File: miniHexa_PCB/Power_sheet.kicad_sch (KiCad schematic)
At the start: 34 parts, among them J2 12v DC, U2 HT7333, U3 RT8289GSP, U4 BQ25886RGE

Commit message: update
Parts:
- removed U2: HT7333, Package_TO_SOT_SMD:SOT-89-3, symbol Regulator_Linear:HT75xx-1-SOT89
- added U6: AMS1117-3.3, Package_TO_SOT_SMD:SOT-223-3_TabPin2, symbol Regulator_Linear:AMS1117-3.3
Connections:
- net +3.3V: now also U6.2 (VO)
- net +5V: now also U6.3 (VI)
- net GND: now also U6.1 (GND)

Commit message: simple update
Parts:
- C11, C12, C14, C15, C16, C17, C18, C19, C20, C21, C22, C23, C24: footprint Capacitor_SMD:C_0805_2012Metric -> Capacitor_SMD:C_0402_1005Metric
- C25: value C -> 4.7uF; footprint Capacitor_SMD:C_0805_2012Metric -> Capacitor_SMD:C_0402_1005Metric
- L1, L2: footprint Inductor_SMD:L_APV_APH0850 -> Inductor_SMD:L_Panasonic_PCC-M0850M
- R27, R28: value R -> 2.2k
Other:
- moved on the sheet: C25
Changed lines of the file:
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@@
 	)
 	(junction
+		(at 257.81 45.72)
+		(diameter 0)
+		(color 0 0 0 0)
+	)
+	(junction
 		(at 52.07 173.99)
 		(diameter 0)
@@
 	)
 	(junction
-		(at 257.81 45.72)
-		(diameter 0)
-		(color 0 0 0 0)
-	)
-	(junction
 		(at 269.24 45.72)
 		(diameter 0)
@@
 	(wire
 		(pts
-			(xy 186.69 55.88) (xy 203.2 55.88)
+			(xy 195.58 55.88) (xy 203.2 55.88)
 		)
 		(stroke
@@
 			)
 		)
-		(property "Footprint" "Capacitor_SMD:C_0805_2012Metric"
+		(property "Footprint" "Capacitor_SMD:C_0402_1005Metric"
 			(at 54.3052 41.91 0)
 			(hide yes)
@@
 			)
 		)
-		(property "Footprint" "Capacitor_SMD:C_0805_2012Metric"
+		(property "Footprint" "Capacitor_SMD:C_0402_1005Metric"
 			(at 73.9648 111.76 0)
 			(hide yes)
@@
 			)
 		)
-		(property "Footprint" "Inductor_SMD:L_APV_APH0850"
+		(property "Footprint" "Inductor_SMD:L_Panasonic_PCC-M0850M"
 			(at 87.63 137.16 0)
 			(hide yes)
@@
 			)
 		)
-		(property "Value" "R"
+		(property "Value" "2.2k"
 			(at 246.38 36.83 90)
 			(show_name no)
@@
 			)
 		)
-		(property "Footprint" "Inductor_SMD:L_APV_APH0850"
+		(property "Footprint" "Inductor_SMD:L_Panasonic_PCC-M0850M"
 			(at 170.18 46.99 0)
 			(hide yes)
@@
 			)
 		)
-		(property "Footprint" "Capacitor_SMD:C_0805_2012Metric"
+		(property "Footprint" "Capacitor_SMD:C_0402_1005Metric"
 			(at 129.54 148.8948 0)
 			(hide yes)
@@
 			)
 		)
-		(property "Footprint" "Capacitor_SMD:C_0805_2012Metric"
+		(property "Footprint" "Capacitor_SMD:C_0402_1005Metric"
 			(at 51.1048 151.13 0)
 			(hide yes)
@@
 			)
 		)
-		(property "Footprint" "Capacitor_SMD:C_0805_2012Metric"
+		(property "Footprint" "Capacitor_SMD:C_0402_1005Metric"
 			(at 62.5348 151.13 0)
 			(hide yes)
@@
 			)
 		)
-		(property "Footprint" "Capacitor_SMD:C_0805_2012Metric"
+		(property "Footprint" "Capacitor_SMD:C_0402_1005Metric"
 			(at 268.2748 45.72 0)
 			(hide yes)
@@
 		(dnp no)
 		(property "Reference" "C20"
-			(at 250.952 48.514 0)
-			(hide yes)
+			(at 252.476 47.752 0)
 			(show_name no)
 			(do_not_autoplace no)
@@
 		)
 		(property "Value" "22uF"
-			(at 251.206 50.8 0)
-			(hide yes)
+			(at 252.73 50.038 0)
 			(show_name no)
 			(do_not_autoplace no)
@@
 			)
 		)
-		(property "Footprint" "Capacitor_SMD:C_0805_2012Metric"
+		(property "Footprint" "Capacitor_SMD:C_0402_1005Metric"
 			(at 256.8448 45.72 0)
 			(hide yes)
@@
 			)
 		)
-		(property "Footprint" "Capacitor_SMD:C_0805_2012Metric"
+		(property "Footprint" "Capacitor_SMD:C_0402_1005Metric"
 			(at 33.9852 41.91 0)
 			(hide yes)
@@
 			)
 		)
-		(property "Footprint" "Capacitor_SMD:C_0805_2012Metric"
+		(property "Footprint" "Capacitor_SMD:C_0402_1005Metric"
 			(at 239.7252 58.42 0)
 			(hide yes)
@@
 	(symbol
 		(lib_id "Device:C")
-		(at 186.69 59.69 0)
+		(at 195.58 59.69 0)
 		(unit 1)
 		(body_style 1)
@@
 		(fields_autoplaced yes)
 		(property "Reference" "C25"
-			(at 190.5 58.4199 0)
+			(at 199.39 58.4199 0)
 			(show_name no)
 			(do_not_autoplace no)
@@
 			)
 		)
-		(property "Value" "C"
-			(at 190.5 60.9599 0)
+		(property "Value" "4.7uF"
+			(at 199.39 60.9599 0)
 			(show_name no)
 			(do_not_autoplace no)
@@
 			)
 		)
-		(property "Footprint" "Capacitor_SMD:C_0805_2012Metric"
-			(at 187.6552 63.5 0)
+		(property "Footprint" "Capacitor_SMD:C_0402_1005Metric"
+			(at 196.5452 63.5 0)
 			(hide yes)
 			(show_name no)
@@
 		)
 		(property "Datasheet" ""
-			(at 186.69 59.69 0)
+			(at 195.58 59.69 0)
 			(hide yes)
 			(show_name no)
@@
 		)
 		(property "Description" "Unpolarized capacitor"
-			(at 186.69 59.69 0)
+			(at 195.58 59.69 0)
 			(hide yes)
 			(show_name no)
@@
 			)
 		)
-		(property "Value" "R"
+		(property "Value" "2.2k"
 			(at 246.38 40.64 90)
 			(show_name no)
@@
 	(symbol
 		(lib_id "power:GND")
-		(at 186.69 63.5 0)
+		(at 195.58 63.5 0)
 		(unit 1)
 		(body_style 1)
@@
 		(fields_autoplaced yes)
 		(property "Reference" "#PWR031"
-			(at 186.69 69.85 0)
+			(at 195.58 69.85 0)
 			(hide yes)
 			(show_name no)
@@
 		)
 		(property "Value" "GND"
-			(at 186.69 68.58 0)
+			(at 195.58 68.58 0)
 			(show_name no)
 			(do_not_autoplace no)
@@
 		)
 		(property "Footprint" ""
-			(at 186.69 63.5 0)
+			(at 195.58 63.5 0)
 			(hide yes)
 			(show_name no)
@@
 		)
 		(property "Datasheet" ""
-			(at 186.69 63.5 0)
+			(at 195.58 63.5 0)
 			(hide yes)
 			(show_name no)
@@
 		)
 		(property "Description" "Power symbol creates a global label with name \"GND\" , ground"
-			(at 186.69 63.5 0)
+			(at 195.58 63.5 0)
 			(hide yes)
 			(show_name no)
@@
 			)
 		)
-		(property "Footprint" "Capacitor_SMD:C_0805_2012Metric"
+		(property "Footprint" "Capacitor_SMD:C_0402_1005Metric"
 			(at 170.18 42.2148 0)
 			(hide yes)
@@
 			)
 		)
-		(property "Footprint" "Capacitor_SMD:C_0805_2012Metric"
+		(property "Footprint" "Capacitor_SMD:C_0402_1005Metric"
 			(at 39.0652 158.75 0)
 			(hide yes)
@@
 			)
 		)
-		(property "Footprint" "Capacitor_SMD:C_0805_2012Metric"
+		(property "Footprint" "Capacitor_SMD:C_0402_1005Metric"
 			(at 85.3948 111.76 0)
 			(hide yes)
@@
 			)
 		)
-		(property "Footprint" "Capacitor_SMD:C_0805_2012Metric"
+		(property "Footprint" "Capacitor_SMD:C_0402_1005Metric"
 			(at 171.1452 58.42 0)
 			(hide yes)

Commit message: layout phase pcb
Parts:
- C19: footprint Capacitor_SMD:C_0402_1005Metric -> Capacitor_SMD:CP_Elec_6.3x7.7
- C22: value C -> 10uF
- C24: value C -> 47nF
- R22, R23, R24, R25, R26, R27, R28, R30, R31: footprint Resistor_SMD:R_0805_2012Metric -> Resistor_SMD:R_0402_1005Metric
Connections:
- net GND: now also C25.1, U4.5 (OTG); no longer C25.2
- net at U4.11 (REGN): now also C25.2; no longer C25.1
- no-connect marks 7 -> 6
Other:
- moved on the sheet: C25
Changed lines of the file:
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@@
 		(at 203.2 59.69)
 	)
-	(no_connect
-		(at 203.2 64.77)
-	)
 	(wire
 		(pts
@@
 			)
 		)
-		(property "Footprint" "Resistor_SMD:R_0805_2012Metric"
+		(property "Footprint" "Resistor_SMD:R_0402_1005Metric"
 			(at 65.532 38.1 90)
 			(hide yes)
@@
 			)
 		)
-		(property "Footprint" "Resistor_SMD:R_0805_2012Metric"
+		(property "Footprint" "Resistor_SMD:R_0402_1005Metric"
 			(at 246.38 38.608 90)
 			(hide yes)
@@
 			)
 		)
-		(property "Footprint" "Resistor_SMD:R_0805_2012Metric"
+		(property "Footprint" "Resistor_SMD:R_0402_1005Metric"
 			(at 196.85 84.328 90)
 			(hide yes)
@@
 	(symbol
 		(lib_id "power:GND")
+		(at 203.2 64.77 270)
+		(unit 1)
+		(body_style 1)
+		(exclude_from_sim no)
+		(in_bom yes)
+		(on_board yes)
+		(in_pos_files yes)
+		(dnp no)
+		(fields_autoplaced yes)
+		(property "Reference" "#PWR032"
+			(at 196.85 64.77 0)
+			(hide yes)
+			(show_name no)
+			(do_not_autoplace no)
+			(effects
+				(font
+					(size 1.27 1.27)
+				)
+			)
+		)
+		(property "Value" "GND"
+			(at 199.39 64.7699 90)
+			(show_name no)
+			(do_not_autoplace no)
+			(effects
+				(font
+					(size 1.27 1.27)
+				)
+				(justify right)
+			)
+		)
+		(property "Footprint" ""
+			(at 203.2 64.77 0)
+			(hide yes)
+			(show_name no)
+			(do_not_autoplace no)
+			(effects
+				(font
+					(size 1.27 1.27)
+				)
+			)
+		)
+		(property "Datasheet" ""
+			(at 203.2 64.77 0)
+			(hide yes)
+			(show_name no)
+			(do_not_autoplace no)
+			(effects
+				(font
+					(size 1.27 1.27)
+				)
+			)
+		)
+		(property "Description" "Power symbol creates a global label with name \"GND\" , ground"
+			(at 203.2 64.77 0)
+			(hide yes)
+			(show_name no)
+			(do_not_autoplace no)
+			(effects
+				(font
+					(size 1.27 1.27)
+				)
+			)
+		)
+		(pin "1"
+		)
+		(instances
+			(project "miniHexa"
+				(path "/3449ee66-2977-4802-a474-0821cdf4e79b/33698118-31e2-44d0-a5be-b46ca646d44a"
+					(reference "#PWR032")
+					(unit 1)
+				)
+			)
+		)
+	)
+	(symbol
+		(lib_id "power:GND")
 		(at 238.76 58.42 0)
 		(unit 1)
@@
 			)
 		)
-		(property "Value" "C"
+		(property "Value" "10uF"
 			(at 233.426 55.372 0)
 			(show_name no)
@@
 	(symbol
 		(lib_id "Device:C")
-		(at 195.58 59.69 0)
+		(at 191.77 55.88 90)
 		(unit 1)
 		(body_style 1)
@@
 		(fields_autoplaced yes)
 		(property "Reference" "C25"
-			(at 199.39 58.4199 0)
+			(at 191.77 48.26 90)
 			(show_name no)
 			(do_not_autoplace no)
@@
 					(size 1.27 1.27)
 				)
-				(justify left)
 			)
 		)
 		(property "Value" "4.7uF"
-			(at 199.39 60.9599 0)
+			(at 191.77 50.8 90)
 			(show_name no)
 			(do_not_autoplace no)
@@
 					(size 1.27 1.27)
 				)
-				(justify left)
 			)
 		)
 		(property "Footprint" "Capacitor_SMD:C_0402_1005Metric"
-			(at 196.5452 63.5 0)
+			(at 195.58 54.9148 0)
 			(hide yes)
 			(show_name no)
@@
 		)
 		(property "Datasheet" ""
-			(at 195.58 59.69 0)
+			(at 191.77 55.88 0)
 			(hide yes)
 			(show_name no)
@@
 		)
 		(property "Description" "Unpolarized capacitor"
-			(at 195.58 59.69 0)
+			(at 191.77 55.88 0)
 			(hide yes)
 			(show_name no)
@@
 			)
 		)
-		(property "Footprint" "Resistor_SMD:R_0805_2012Metric"
+		(property "Footprint" "Resistor_SMD:R_0402_1005Metric"
 			(at 246.38 42.418 90)
 			(hide yes)
@@
 			)
 		)
-		(property "Footprint" "Resistor_SMD:R_0805_2012Metric"
+		(property "Footprint" "Resistor_SMD:R_0402_1005Metric"
 			(at 71.882 162.56 90)
 			(hide yes)
@@
 	(symbol
 		(lib_id "power:GND")
-		(at 195.58 63.5 0)
+		(at 187.96 55.88 0)
 		(unit 1)
 		(body_style 1)
@@
 		(fields_autoplaced yes)
 		(property "Reference" "#PWR031"
-			(at 195.58 69.85 0)
+			(at 187.96 62.23 0)
 			(hide yes)
 			(show_name no)
@@
 		)
 		(property "Value" "GND"
-			(at 195.58 68.58 0)
+			(at 187.96 60.96 0)
 			(show_name no)
 			(do_not_autoplace no)
@@
 		)
 		(property "Footprint" ""
-			(at 195.58 63.5 0)
+			(at 187.96 55.88 0)
 			(hide yes)
 			(show_name no)
@@
 		)
 		(property "Datasheet" ""
-			(at 195.58 63.5 0)
+			(at 187.96 55.88 0)
 			(hide yes)
 			(show_name no)
@@
 		)
 		(property "Description" "Power symbol creates a global label with name \"GND\" , ground"
-			(at 195.58 63.5 0)
+			(at 187.96 55.88 0)
 			(hide yes)
 			(show_name no)
@@
 			)
 		)
-		(property "Footprint" "Resistor_SMD:R_0805_2012Metric"
+		(property "Footprint" "Resistor_SMD:R_0402_1005Metric"
 			(at 71.882 147.32 90)
 			(hide yes)
@@
 			)
 		)
-		(property "Footprint" "Resistor_SMD:R_0805_2012Metric"
+		(property "Footprint" "Resistor_SMD:R_0402_1005Metric"
 			(at 125.73 106.172 90)
 			(hide yes)
@@
 			)
 		)
-		(property "Footprint" "Resistor_SMD:R_0805_2012Metric"
+		(property "Footprint" "Resistor_SMD:R_0402_1005Metric"
 			(at 196.85 79.248 90)
 			(hide yes)
@@
 			)
 		)
-		(property "Footprint" "Capacitor_SMD:C_0402_1005Metric"
+		(property "Footprint" "Capacitor_SMD:CP_Elec_6.3x7.7"
 			(at 39.0652 158.75 0)
 			(hide yes)
@@
 			)
 		)
-		(property "Footprint" "Resistor_SMD:R_0805_2012Metric"
+		(property "Footprint" "Resistor_SMD:R_0402_1005Metric"
 			(at 196.85 74.168 90)
 			(hide yes)
@@
 			)
 		)
-		(property "Value" "C"
+		(property "Value" "47nF"
 			(at 162.814 55.372 0)
 			(show_name no)

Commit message: before auto routing
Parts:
- added C2: 22uF, Capacitor_SMD:C_0402_1005Metric, symbol Device:C
- added C27: 100nF, Capacitor_SMD:C_0402_1005Metric, symbol Device:C
- BT1: footprint Battery:BatteryHolder_Keystone_2468_2xAAA -> Connector_JST:JST_XH_S2B-XH-A-1_1x02_P2.50mm_Horizontal
- C23: value C -> 10uF
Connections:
- net GND: now also C2.1, C27.1
- net at J2.1, U4.23 (VBUS): now also C2.2, C27.2

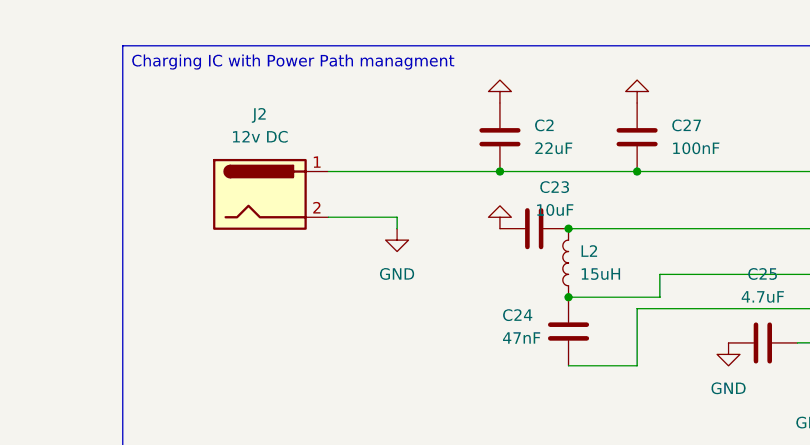
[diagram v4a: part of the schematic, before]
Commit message: added water marks
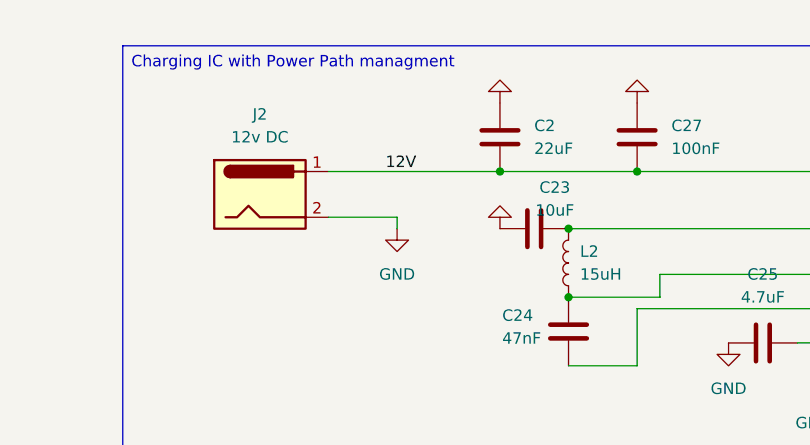
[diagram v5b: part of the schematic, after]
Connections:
- net 12V: now reaches C2.2, C27.2, J2.1, U4.23 (VBUS)
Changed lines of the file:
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@@
+		)
+	)
+	(label "12V"
+		(at 149.8505 36.83 0)
+		(effects
+			(font
+				(size 1.27 1.27)
+			)
+			(justify left bottom)
 		)
 	)

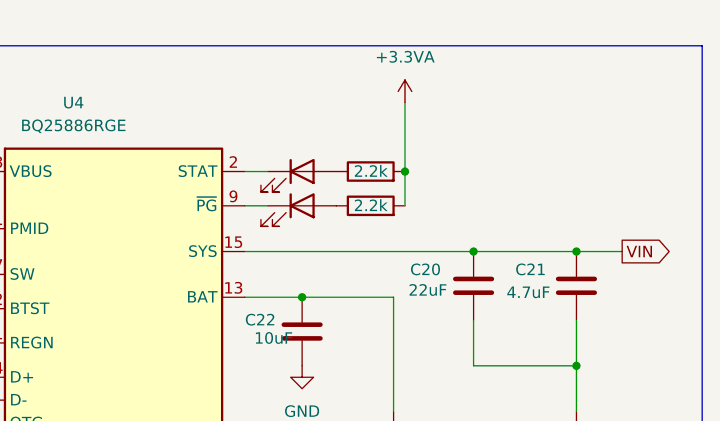
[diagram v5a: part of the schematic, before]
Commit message: updated some power lines
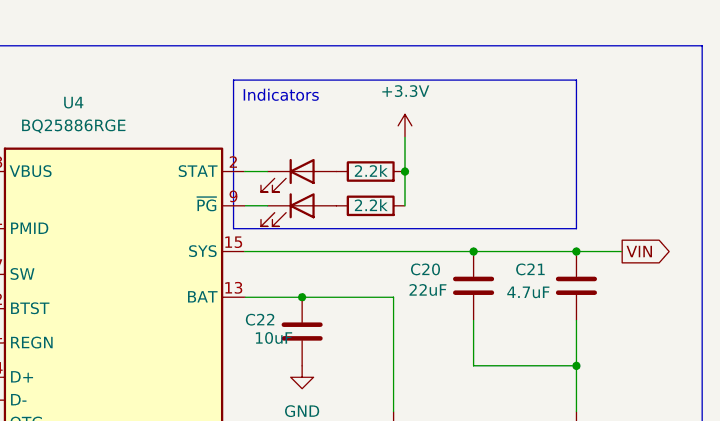
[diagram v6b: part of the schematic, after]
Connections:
- net +3.3VA is gone; now on net +3.3V: R27.2, R28.2
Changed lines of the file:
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@@
 		)
 	)
+	(text_box "Indicators"
+		(exclude_from_sim no)
+		(at 231.14 26.67 0)
+		(size 38.1 16.51)
+		(margins 0.9525 0.9525 0.9525 0.9525)
+		(stroke
+			(width 0)
+			(type solid)
+		)
+		(fill
+			(type none)
+		)
+		(effects
+			(font
+				(size 1.27 1.27)
+			)
+			(justify left top)
+		)
+	)
 	(junction
 		(at 53.34 41.91)
@@
 	)
 	(junction
-		(at 162.56 36.83)
+		(at 250.19 36.83)
 		(diameter 0)
 		(color 0 0 0 0)
 	)
 	(junction
-		(at 170.18 50.8)
+		(at 162.56 36.83)
 		(diameter 0)
 		(color 0 0 0 0)
 	)
 	(junction
-		(at 63.5 173.99)
+		(at 170.18 50.8)
 		(diameter 0)
 		(color 0 0 0 0)
 	)
 	(junction
-		(at 269.24 58.42)
+		(at 63.5 173.99)
 		(diameter 0)
 		(color 0 0 0 0)
 	)
 	(junction
-		(at 250.19 36.83)
+		(at 269.24 58.42)
 		(diameter 0)
 		(color 0 0 0 0)
@@
 	(wire
 		(pts
-			(xy 250.19 29.21) (xy 250.19 36.83)
+			(xy 250.19 33.02) (xy 250.19 36.83)
 		)
 		(stroke
@@
 	)
 	(symbol
+		(lib_id "power:+3.3V")
+		(at 250.19 33.02 0)
+		(unit 1)
+		(body_style 1)
+		(exclude_from_sim no)
+		(in_bom yes)
+		(on_board yes)
+		(in_pos_files yes)
+		(dnp no)
+		(fields_autoplaced yes)
+		(property "Reference" "#PWR022"
+			(at 250.19 36.83 0)
+			(hide yes)
+			(show_name no)
+			(do_not_autoplace no)
+			(effects
+				(font
+					(size 1.27 1.27)
+				)
+			)
+		)
+		(property "Value" "+3.3V"
+			(at 250.19 27.94 0)
+			(show_name no)
+			(do_not_autoplace no)
+			(effects
+				(font
+					(size 1.27 1.27)
+				)
+			)
+		)
+		(property "Footprint" ""
+			(at 250.19 33.02 0)
+			(hide yes)
+			(show_name no)
+			(do_not_autoplace no)
+			(effects
+				(font
+					(size 1.27 1.27)
+				)
+			)
+		)
+		(property "Datasheet" ""
+			(at 250.19 33.02 0)
+			(hide yes)
+			(show_name no)
+			(do_not_autoplace no)
+			(effects
+				(font
+					(size 1.27 1.27)
+				)
+			)
+		)
+		(property "Description" "Power symbol creates a global label with name \"+3.3V\""
+			(at 250.19 33.02 0)
+			(hide yes)
+			(show_name no)
+			(do_not_autoplace no)
+			(effects
+				(font
+					(size 1.27 1.27)
+				)
+			)
+		)
+		(pin "1"
+		)
+		(instances
+			(project "miniHexa"
+				(path "/3449ee66-2977-4802-a474-0821cdf4e79b/33698118-31e2-44d0-a5be-b46ca646d44a"
+					(reference "#PWR022")
+					(unit 1)
+				)
+			)
+		)
+	)
+	(symbol
 		(lib_id "Device:L")
 		(at 87.63 137.16 90)
@@
 					(unit 1)
 				)
-			)
-		)
-	)
-	(symbol
-		(lib_id "power:+3.3VA")
-		(at 250.19 29.21 0)
-		(unit 1)
-		(body_style 1)
-		(exclude_from_sim no)
-		(in_bom yes)
-		(on_board yes)
-		(in_pos_files yes)
-		(dnp no)
-		(fields_autoplaced yes)
-		(property "Reference" "#PWR028"
-			(at 250.19 33.02 0)
-			(hide yes)
-			(show_name no)
-			(do_not_autoplace no)
-			(effects
-				(font
-					(size 1.27 1.27)
-				)
-			)
-		)
-		(property "Value" "+3.3VA"
-			(at 250.19 24.13 0)
-			(show_name no)
-			(do_not_autoplace no)
-			(effects
-				(font
-					(size 1.27 1.27)
-				)
-			)
-		)
-		(property "Footprint" ""
-			(at 250.19 29.21 0)
-			(hide yes)
-			(show_name no)
-			(do_not_autoplace no)
-			(effects
-				(font
-					(size 1.27 1.27)
-				)
-			)
-		)
-		(property "Datasheet" ""
-			(at 250.19 29.21 0)
-			(hide yes)
-			(show_name no)
-			(do_not_autoplace no)
-			(effects
-				(font
-					(size 1.27 1.27)
-				)
-			)
-		)
-		(property "Description" "Power symbol creates a global label with name \"+3.3VA\""
-			(at 250.19 29.21 0)
-			(hide yes)
-			(show_name no)
-			(do_not_autoplace no)
-			(effects
-				(font
-					(size 1.27 1.27)
-				)
-			)
-		)
-		(pin "1"
-		)
-		(instances
-			(project "miniHexa"
-				(path "/3449ee66-2977-4802-a474-0821cdf4e79b/33698118-31e2-44d0-a5be-b46ca646d44a"
-					(reference "#PWR028")
-					(unit 1)
-				)

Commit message: tried to make it cleaner
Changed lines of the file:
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@@
 		(dnp no)
 		(property "Reference" "C22"
-			(at 232.41 53.34 0)
+			(at 234.188 66.04 0)
 			(show_name no)
 			(do_not_autoplace no)
@@
 		)
 		(property "Value" "10uF"
-			(at 233.426 55.372 0)
+			(at 235.204 68.072 0)
 			(show_name no)
 			(do_not_autoplace no)

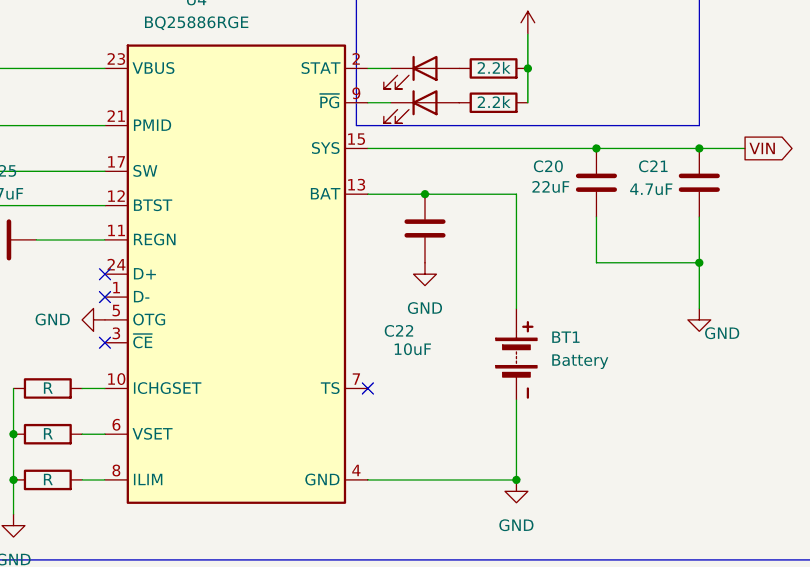
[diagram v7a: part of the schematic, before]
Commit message: changed footprint for pol cap; Need to adjust font size for the silk screen
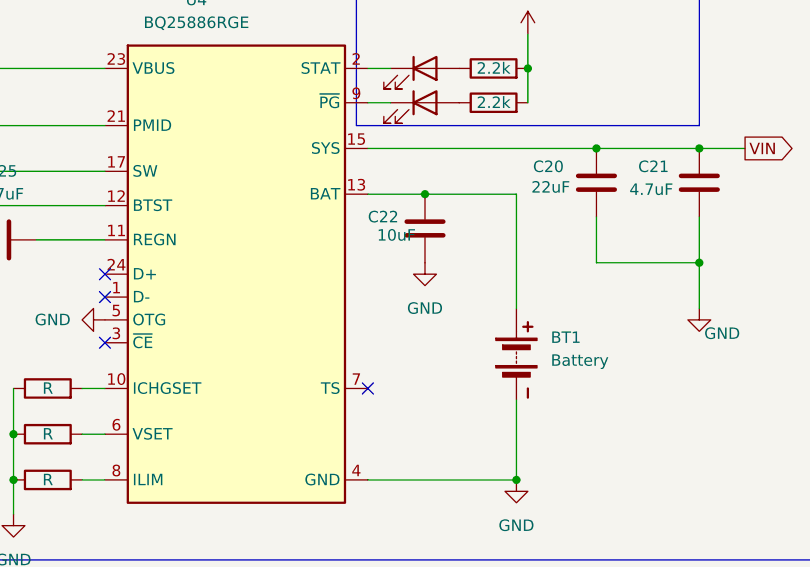
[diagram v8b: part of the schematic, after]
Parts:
- C19: footprint Capacitor_SMD:CP_Elec_6.3x7.7 -> Capacitor_SMD:CP_Elec_5x5.4
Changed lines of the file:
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@@
 		(dnp no)
 		(property "Reference" "C22"
-			(at 234.188 66.04 0)
+			(at 232.41 53.34 0)
 			(show_name no)
 			(do_not_autoplace no)
@@
 		)
 		(property "Value" "10uF"
-			(at 235.204 68.072 0)
+			(at 233.426 55.372 0)
 			(show_name no)
 			(do_not_autoplace no)
@@
 			)
 		)
-		(property "Footprint" "Capacitor_SMD:CP_Elec_6.3x7.7"
+		(property "Footprint" "Capacitor_SMD:CP_Elec_5x5.4"
 			(at 39.0652 158.75 0)
 			(hide yes)
